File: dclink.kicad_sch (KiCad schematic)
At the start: 2 parts, among them U1 mounting_holes, U2 dcb-310

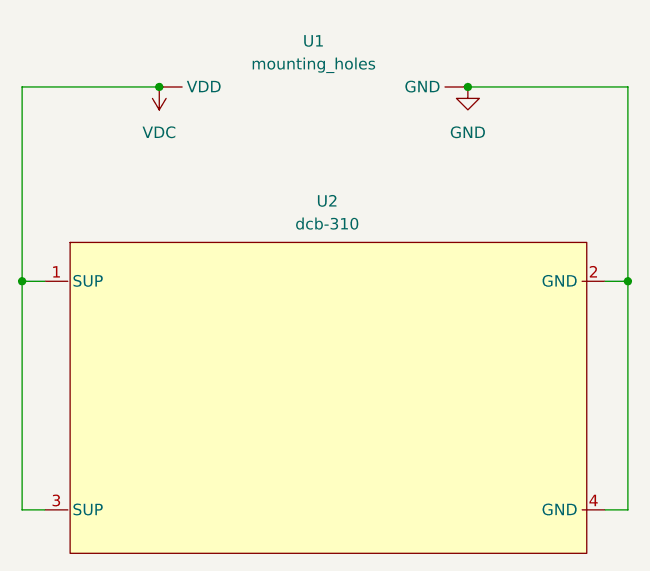
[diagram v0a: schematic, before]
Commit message: add footprint capacitor
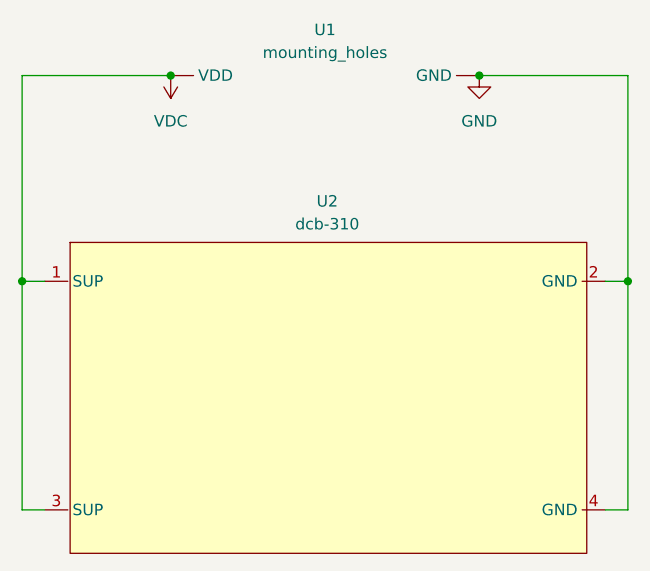
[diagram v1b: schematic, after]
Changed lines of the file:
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@@
     (company "E-Agle TRT")
   )
-  (junction (at 111.76 63.5) (diameter 0) (color 0 0 0 0)
+  (junction (at 113.03 62.23) (diameter 0) (color 0 0 0 0)
   )
   (junction (at 96.52 85.09) (diameter 0) (color 0 0 0 0)
   )
-  (junction (at 146.05 63.5) (diameter 0) (color 0 0 0 0)
+  (junction (at 147.32 62.23) (diameter 0) (color 0 0 0 0)
   )
   (junction (at 163.83 85.09) (diameter 0) (color 0 0 0 0)
   )
-  (wire (pts (xy 163.83 63.5) (xy 163.83 85.09))
+  (wire (pts (xy 163.83 62.23) (xy 163.83 85.09))
     (stroke (width 0) (type default) (color 0 0 0 0))
   )
@@
     (stroke (width 0) (type default) (color 0 0 0 0))
   )
+  (wire (pts (xy 161.29 85.09) (xy 163.83 85.09))
+    (stroke (width 0) (type default) (color 0 0 0 0))
+  )
+  (wire (pts (xy 96.52 85.09) (xy 96.52 110.49))
+    (stroke (width 0) (type default) (color 0 0 0 0))
+  )
   (wire (pts (xy 96.52 110.49) (xy 99.06 110.49))
     (stroke (width 0) (type default) (color 0 0 0 0))
   )
-  (wire (pts (xy 161.29 85.09) (xy 163.83 85.09))
+  (wire (pts (xy 147.32 62.23) (xy 163.83 62.23))
     (stroke (width 0) (type default) (color 0 0 0 0))
   )
-  (wire (pts (xy 146.05 63.5) (xy 163.83 63.5))
+  (wire (pts (xy 96.52 62.23) (xy 96.52 85.09))
     (stroke (width 0) (type default) (color 0 0 0 0))
   )
-  (wire (pts (xy 96.52 63.5) (xy 96.52 85.09))
+  (wire (pts (xy 161.29 110.49) (xy 163.83 110.49))
+    (stroke (width 0) (type default) (color 0 0 0 0))
+  )
+  (wire (pts (xy 113.03 62.23) (xy 96.52 62.23))
     (stroke (width 0) (type default) (color 0 0 0 0))
   )
@@
     (stroke (width 0) (type default) (color 0 0 0 0))
   )
-  (wire (pts (xy 111.76 63.5) (xy 96.52 63.5))
-    (stroke (width 0) (type default) (color 0 0 0 0))
-  )
-  (wire (pts (xy 96.52 85.09) (xy 96.52 110.49))
-    (stroke (width 0) (type default) (color 0 0 0 0))
-  )
-  (wire (pts (xy 163.83 110.49) (xy 161.29 110.49))
-    (stroke (width 0) (type default) (color 0 0 0 0))
-  )
-  (symbol (lib_id "power:GND") (at 146.05 63.5 0) (unit 1)
-    (in_bom yes) (on_board yes) (fields_autoplaced)
-    (property "Reference" "#PWR0101" (id 0) (at 146.05 69.85 0)
+  (symbol (lib_id "power:VDC") (at 113.03 62.23 180) (unit 1)
+    (in_bom yes) (on_board yes)
+    (property "Reference" "#PWR01" (id 0) (at 113.03 59.69 0)
       (effects (font (size 1.27 1.27)) hide)
     )
-    (property "Value" "GND" (id 1) (at 146.05 68.58 0))
-    (property "Footprint" "" (id 2) (at 146.05 63.5 0)
+    (property "Value" "VDC" (id 1) (at 113.03 67.31 0))
+    (property "Footprint" "" (id 2) (at 113.03 62.23 0)
       (effects (font (size 1.27 1.27)) hide)
     )
-    (property "Datasheet" "" (id 3) (at 146.05 63.5 0)
+    (property "Datasheet" "" (id 3) (at 113.03 62.23 0)
       (effects (font (size 1.27 1.27)) hide)
     )
     (pin "1")
   )
-  (symbol (lib_id "power:VDC") (at 111.76 63.5 180) (unit 1)
+  (symbol (lib_id "power:GND") (at 147.32 62.23 0) (unit 1)
     (in_bom yes) (on_board yes) (fields_autoplaced)
-    (property "Reference" "#PWR0102" (id 0) (at 111.76 60.96 0)
+    (property "Reference" "#PWR02" (id 0) (at 147.32 68.58 0)
       (effects (font (size 1.27 1.27)) hide)
     )
-    (property "Value" "VDC" (id 1) (at 111.76 68.58 0))
-    (property "Footprint" "" (id 2) (at 111.76 63.5 0)
+    (property "Value" "GND" (id 1) (at 147.32 67.31 0))
+    (property "Footprint" "" (id 2) (at 147.32 62.23 0)
       (effects (font (size 1.27 1.27)) hide)
     )
-    (property "Datasheet" "" (id 3) (at 111.76 63.5 0)
+    (property "Datasheet" "" (id 3) (at 147.32 62.23 0)
       (effects (font (size 1.27 1.27)) hide)
     )
     (pin "1")
-  )
-  (symbol (lib_name "mounting_holes_1") (lib_id "dcbk310:mounting_holes") (at 128.27 63.5 0) (unit 1)
-    (in_bom yes) (on_board yes) (fields_autoplaced)
-    (property "Reference" "U1" (id 0) (at 128.905 58.42 0))
-    (property "Value" "mounting_holes" (id 1) (at 128.905 60.96 0))
-    (property "Footprint" "dcbk310:mounting_holes" (id 2) (at 128.27 63.5 0)
-      (effects (font (size 1.27 1.27)) hide)
-    )
-    (property "Datasheet" "" (id 3) (at 128.27 63.5 0)
-      (effects (font (size 1.27 1.27)) hide)
-    )
-    (pin "")
-    (pin "")
   )
   (symbol (lib_id "dcbk310:dcb-310") (at 132.08 95.25 0) (unit 1)
@@
     (pin "4")
   )
+  (symbol (lib_id "dcbk310:mounting_holes") (at 129.54 62.23 0) (unit 1)
+    (in_bom yes) (on_board yes) (fields_autoplaced)
+    (property "Reference" "U1" (id 0) (at 130.175 57.15 0))
+    (property "Value" "mounting_holes" (id 1) (at 130.175 59.69 0))
+    (property "Footprint" "dcbk310:mounting_holes" (id 2) (at 129.54 62.23 0)
+      (effects (font (size 1.27 1.27)) hide)
+    )
+    (property "Datasheet" "" (id 3) (at 129.54 62.23 0)
+      (effects (font (size 1.27 1.27)) hide)
+    )
+    (pin "")
+    (pin "")
+  )
   (sheet_instances
     (path "/" (page "1"))
   )
   (symbol_instances
-    (path "/06bccb0b-2f4b-4092-834b-3871294199da"
-      (reference "#PWR0101") (unit 1) (value "GND") (footprint "")
+    (path "/1f308c3e-474c-4877-8ef7-b8a073e3c94f"
+      (reference "#PWR01") (unit 1) (value "VDC") (footprint "")
     )
-    (path "/119a2ba9-03f2-48af-8f1a-4a96cb25a3bf"
-      (reference "#PWR0102") (unit 1) (value "VDC") (footprint "")
+    (path "/8f11fd72-48f8-41ba-b401-54b8b3794a9f"
+      (reference "#PWR02") (unit 1) (value "GND") (footprint "")
     )
-    (path "/5b29962f-685a-409c-915c-9c4a92ed442a"
+    (path "/ceec7167-0834-4472-b45d-d666f60ac721"
       (reference "U1") (unit 1) (value "mounting_holes") (footprint "dcbk310:mounting_holes")
     )
-    (path "/8f6e655b-cbc6-42da-bb7f-c7fcd17f3d2f"
+    (path "/a82435ab-0c66-43c0-b538-8f19bb28d5ea"
       (reference "U2") (unit 1) (value "dcb-310") (footprint "dcbk310:dcb-k310")
     )
